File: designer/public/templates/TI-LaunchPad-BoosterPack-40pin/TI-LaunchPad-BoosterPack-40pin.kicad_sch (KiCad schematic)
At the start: 2 parts, among them J2-J4 Conn_01x10, J3-J1 Conn_01x10

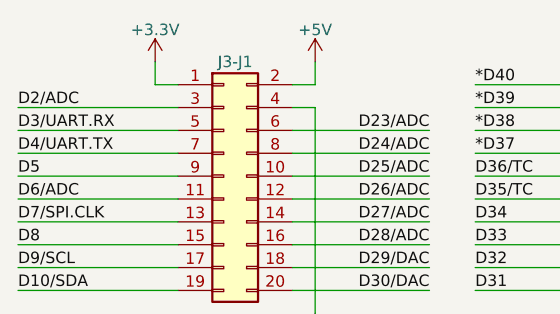
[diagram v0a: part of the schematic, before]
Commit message: designer: make the project manager indistinguishable from KiCad's
An engineer arriving from KiCad should not be able to tell the two windows
apart. This is that pass over the manager frame, ported from the 10.0.5 source
the user runs rather than from screenshots, with the screenshots used only to
settle the colours GTK paints rather than KiCad.

The palette drops the blue tint it had for the neutral greys the theme
actually uses, and the shell adopts wxSYS_DEFAULT_GUI_FONT's 11pt in the menu
bar, tree, launcher, status bar, buttons and dialog headers.

PANEL_KICAD_LAUNCHER: the tile order and tooltips come from CreateLaunchers(),
the New Project icon is new_project_from_template as KICAD_MANAGER_ACTIONS
names it, and the hover box is the 56px button - a 48px bitmap plus
SetPadding(4) - not the 760px row, so hovering the label no longer lights it.
BITMAP_BUTTON::OnPaint draws a rectangle, hence the square corners. The Plugin
and Content Manager tile and its menu entry are gone for now.

PROJECT_TREE_PANE: selection hugs the icon and label rather than the row,
because wxTR_FULL_ROW_HIGHLIGHT appears nowhere in KiCad; single click
selects and only double click expands; and the file list is
s_allowedExtensionsToList transcribed, an allow list with no .step or .wrl -
which is why a .3dshapes folder gets no expander. The pane width persists as
m_LeftWinWidth does.

KISTATUSBAR ellipsizes the middle of the project path the way
SetEllipsedTextField does, minus the width of "XX"; ellipsize.ts is that
wxELLIPSIZE_MIDDLE port.

DIALOG_TEMPLATE_SELECTOR is rebuilt against 10.0.5, which differs from master
here: three filter choices rather than four, no Browse/Clear row, and cards
labelled with the template's directory name, because PROJECT_TEMPLATE's
constructor assigns m_title = GetPrjDirName() and leaves GetTitle()'s HTML
parse unreachable. tools/templates/import.mjs derives title, description and
file list the same three ways the C++ does and imports all 20 templates with
th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
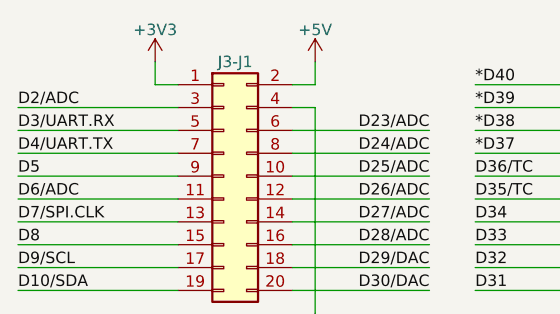
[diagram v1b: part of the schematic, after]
